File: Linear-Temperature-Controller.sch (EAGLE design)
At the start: 78 parts, among them IC1 LM393D, IC3 AD5624R, IC4 AD5262, IC5 LF356MX, T1 MMBT3904, T2 MMBT3904

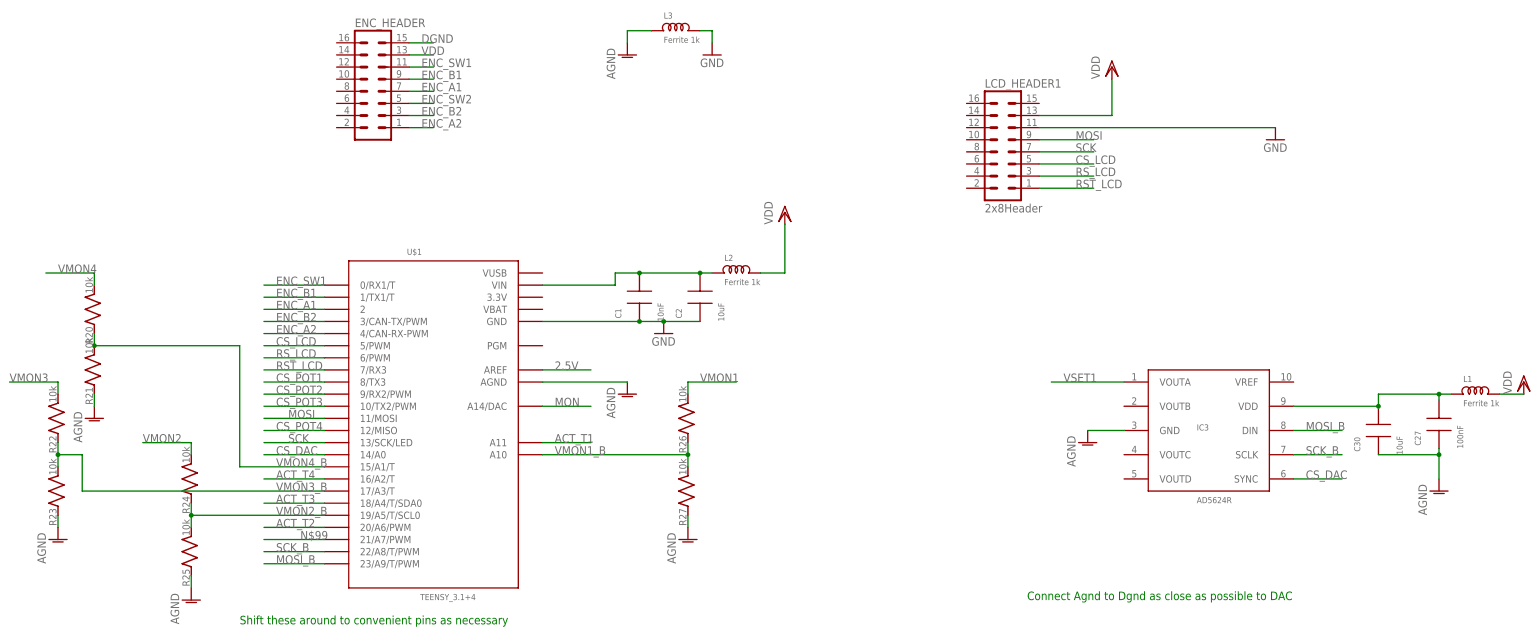
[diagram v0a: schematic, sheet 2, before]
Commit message: Fix minor errors on prototype schematic
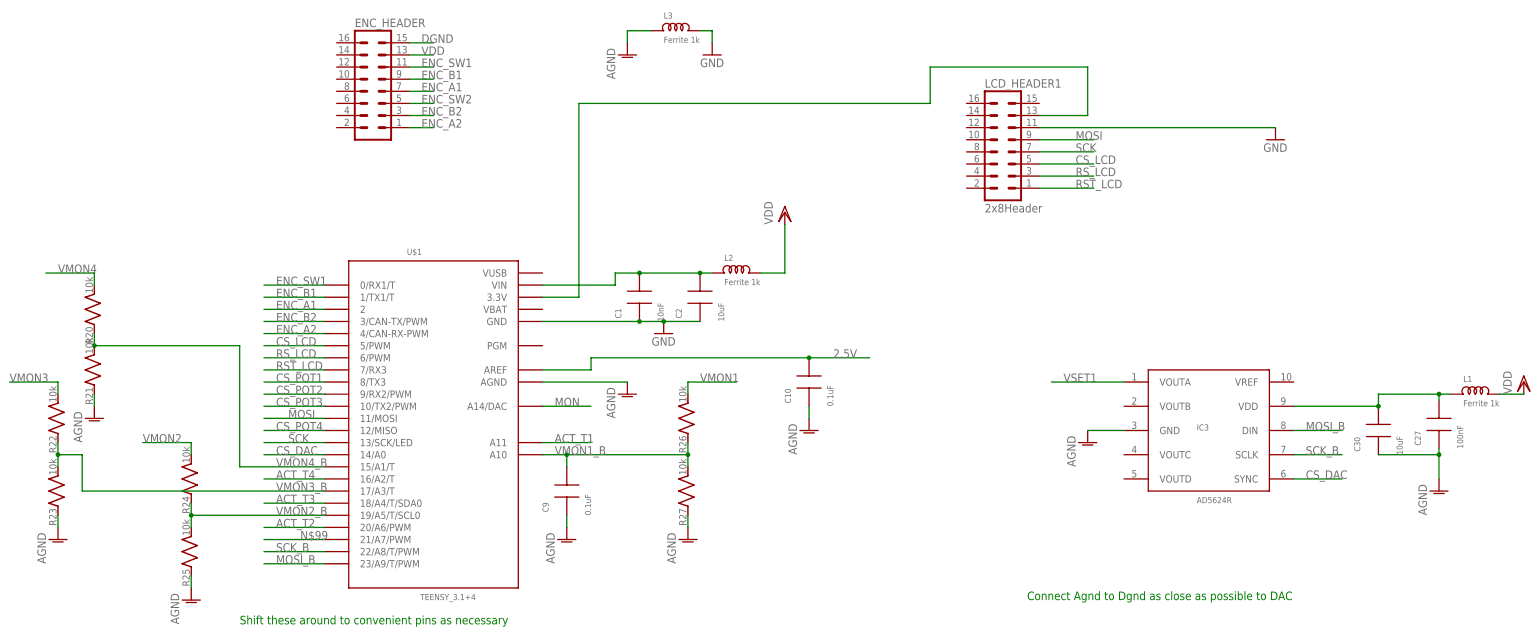
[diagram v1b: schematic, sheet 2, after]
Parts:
- added C10, C9: 0.1uF, rlc-jqi:CAP0805
- R11: value 10k -> 33k
- R8: value 33k -> 10k
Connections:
- new net N$21: LCD_HEADER1.13, U$1.3.3V
- net 2.5V: now also C10.P$2
- net AGND: now also C10.P$1, C9.P$1
- net N$23: no longer U1.8/SG
- net N$6: now also IC1A.-IN; no longer IC1A.+IN
- net N$7: now also IC1B.+IN; no longer IC1B.-IN
- net VDD: now also IC4.PR, IC4.SHDN; no longer LCD_HEADER1.13
- net VMON1_B: now also C9.P$2
- net VSET1: now also IC1A.+IN, IC1B.-IN; no longer IC1A.-IN, IC1B.+IN
